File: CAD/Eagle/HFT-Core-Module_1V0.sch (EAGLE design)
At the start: 295 parts, among them Q0521 ABS07-32.768KHZ, Q0911 ABM3B-16MHZ-10-R50-1-U, U0111 STM32L4Z_144PIN_SMPS, U0431 PAM2305AAB120, U0601 LM4120IM5-3.0, U0611 MAX5217, U0631 CFPT-141-20MHZ, U0641 OPA354, U0701 SI5338, U0801 NHD-C0220BIZ_2X20CHARS, U0901 AX5243, U1001 AX5243, U1111 MAX5136AGTG+, U1121 OPA354, U1131 OPA354, U1141 OPA354, U1601 SOLARPANEL_3V3_5MA1_25MM_X_20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, U1602 SPV1040T, U1701 TS5A23166, U1801 PAM2305AAB330, U1901 TS5A23166, U2001 TS5A23166, U2101 TS5A23166, X1501 CUI SJ1-3535NS, X1511 CUI SJ1-3535NS, X511 2X20/90_1MM27_HARWIN_M50-3202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, X512 2X20/90_1MM27_HARWIN_M50-3202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, X521 2X20/90_1MM27_HARWIN_M50-3202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, X522 2X20/90_1MM27_HARWIN_M50-3202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, X531 2X20/90_1MM27_HARWIN_M50-3202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, X532 2X20/90_1MM27_HARWIN_M50-3202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

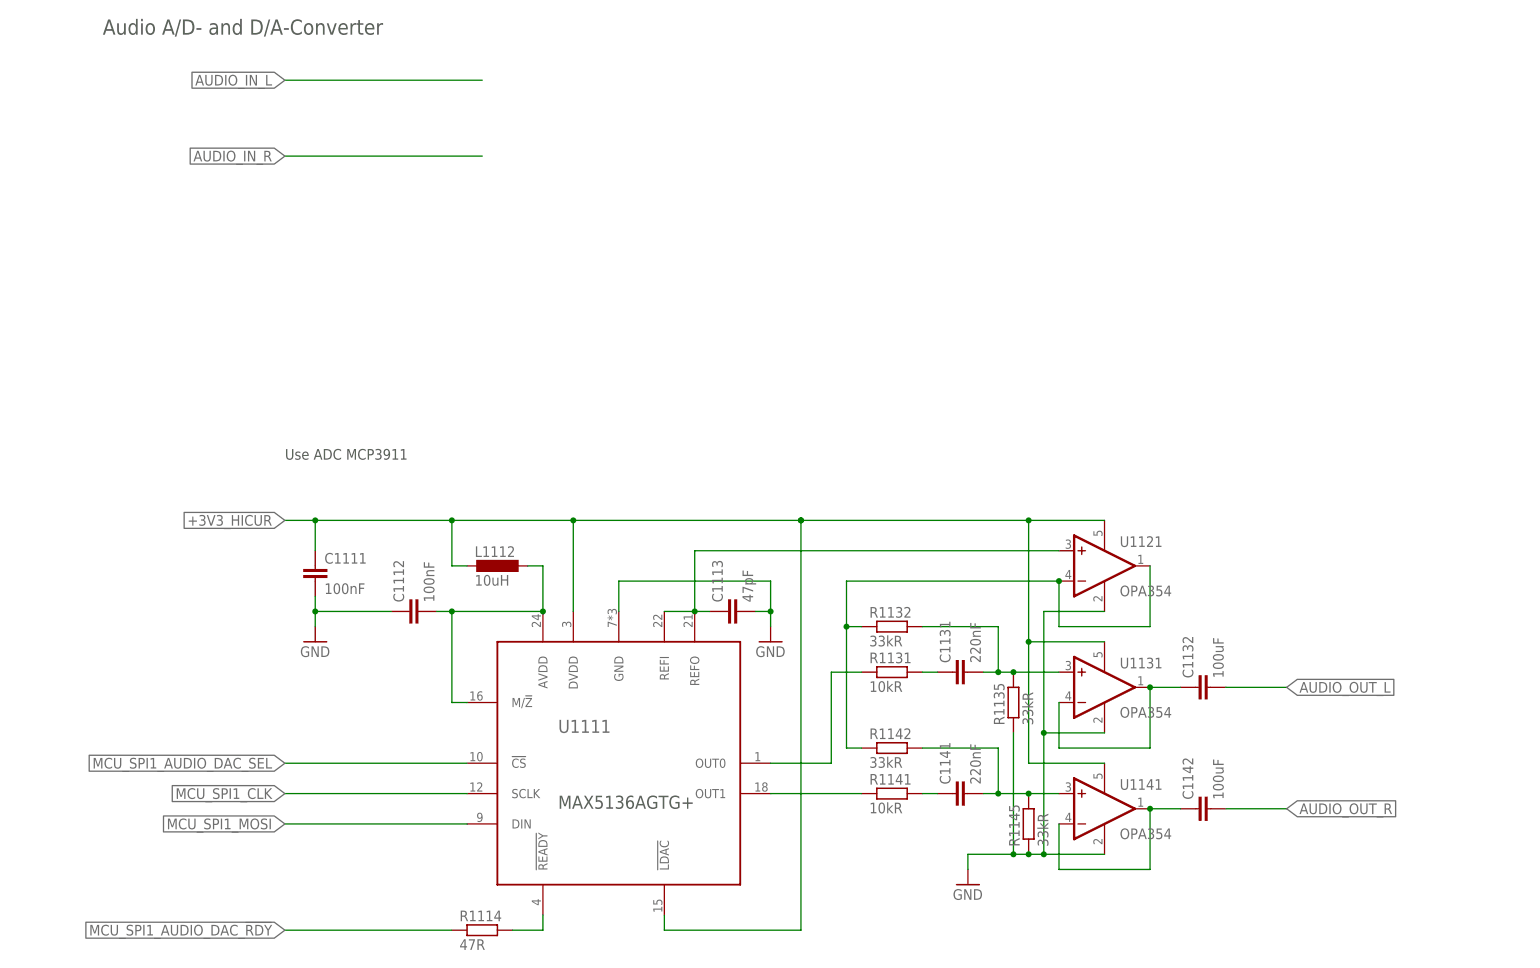
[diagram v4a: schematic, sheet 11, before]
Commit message: HW_1V0 - Audio ADC added
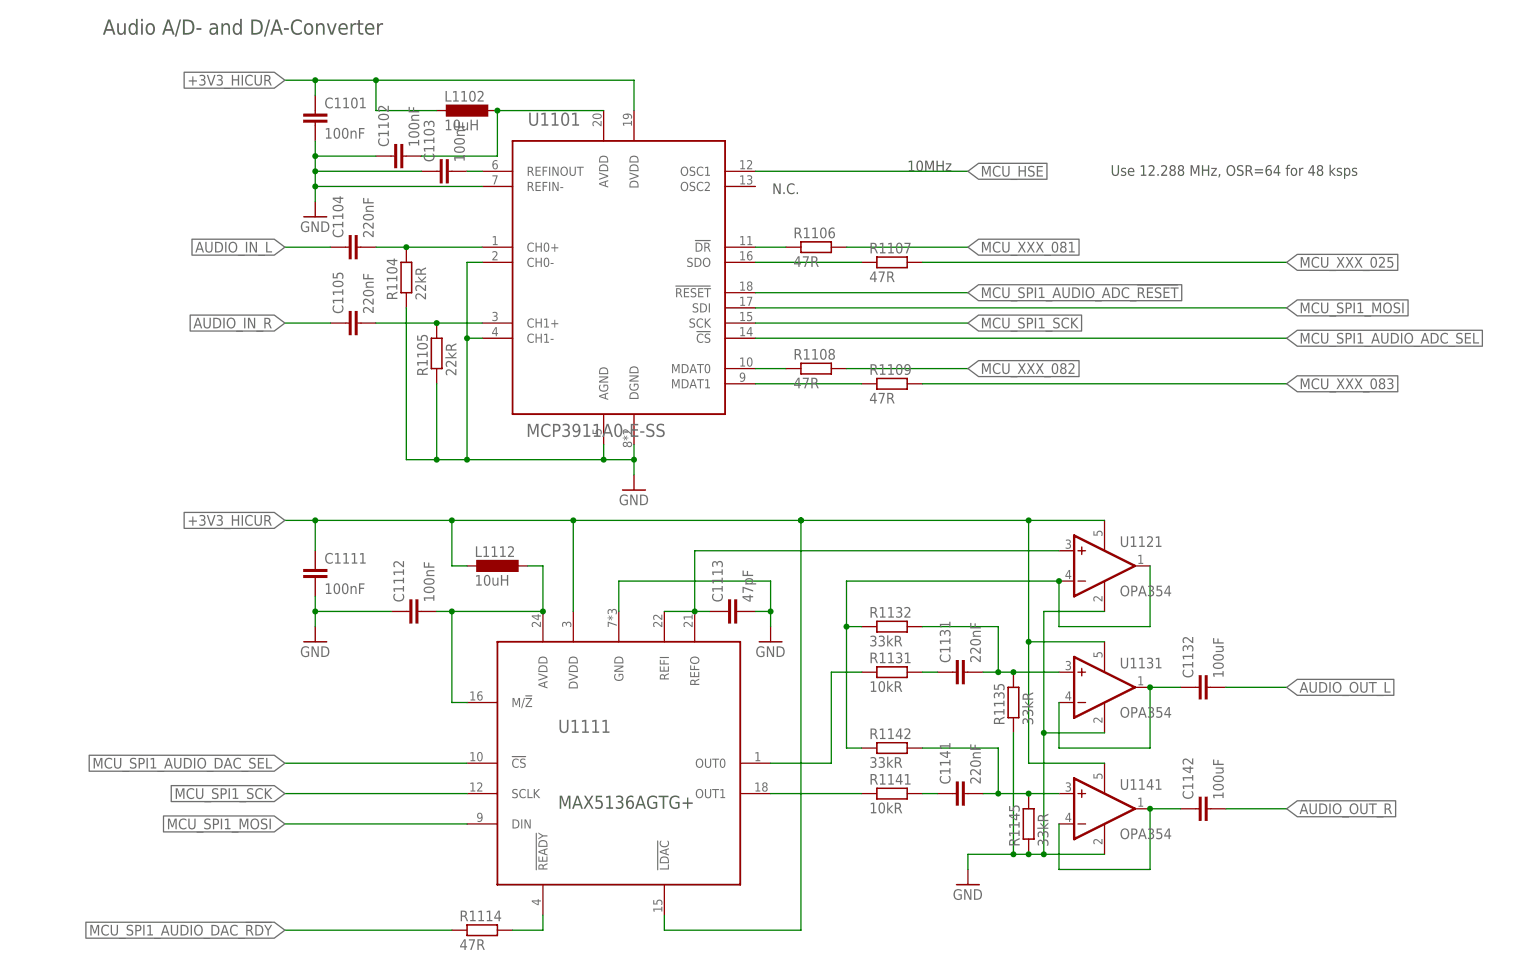
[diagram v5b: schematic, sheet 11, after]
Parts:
- removed R0841: 47R, rcl:R-EU_R0603
- added C1101, C1102, C1103: 100nF, rcl:C-EUC0603
- added C1104, C1105: 220nF, df4iah_rcl:C-EUC0603
- added L1102: 10uH, rcl:L-EUL2012C
- added R0003, R0004, R1106, R1107, R1108, R1109: 47R, rcl:R-EU_R0603
- added R1104, R1105: 22kR, rcl:R-EU_R0603
- added U1101: MCP3911A0-E-SS, df4iah_adc:MCP3911
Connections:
- net N$1 renamed MAX5217_!AUX
- removed net LCD_!RST: R0841.1, U0801.RST
- removed net MCU_SPI1_CLK: R0211.2, U0901.CLK, U1001.CLK, U1111.SCLK
- new net MCP3911_!DR: R1106.1, U1101.!DR
- new net MCP3911_CH0+: C1104.2, R1104.2, U1101.CH0+
- new net MCP3911_CH1+: C1105.2, R1105.2, U1101.CH1+
- new net MCP3911_MDAT0: R1108.1, U1101.MDAT0
- new net MCP3911_MDAT1: R1109.1, U1101.MDAT1
- new net MCP3911_REFINOUT: C1103.2, U1101.REFINOUT
- new net MCP3911_SDO: R1107.1, U1101.SDO
- new net MCU_SPI1_AUDIO_ADC_!RESET: R0003.2, U1101.!RESET
- new net MCU_SPI1_AUDIO_ADC_SEL: R0004.2, U1101.!CS
- new net MCU_SPI1_SCK: R0211.2, U0901.CLK, U1001.CLK, U1101.SCK, U1111.SCLK
- new net MCU_XXX_081: R1106.2
- new net MCU_XXX_082: R1108.2
- new net MCU_XXX_083: R1109.2
- new net MCU_XXX_084: R0003.1
- new net MCU_XXX_085: R0004.1
- new net MVP3911_AVDD: C1102.2, L1102.1, U1101.AVDD
- net +3V3_HICUR: now also C1101.1, L1102.2, U1101.DVDD
- net AUDIO_IN_L: now also C1104.1
- net AUDIO_IN_R: now also C1105.1
- net GND: now also C1101.2, C1102.1, C1103.1, R1104.1, R1105.1, U1101.AGND, U1101.CH0-, U1101.CH1-, U1101.DGND, U1101.REFIN-
- net MCU_HSE: now also U1101.OSC1
- net MCU_LCD_!RST: now also U0801.RST; no longer R0841.2
- net MCU_SPI1_MOSI: now also U1101.SDI
- net MCU_XXX_025: now also R1107.2
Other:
- note added: "10MHz"
- note added: "16MHz"
- note added: "20MHz"
- note added: "MCU_SPI1_AUDIO_ADC_!DR"
- note added: "MCU_SPI1_AUDIO_ADC_M0"
- note added: "MCU_SPI1_AUDIO_ADC_M1"
- note added: "N.C."
- note added: "Use 12.288 MHz, OSR=64 for 48 ksps"
- note removed: "Use ADC MCP3911"
- moved on the sheet: R0642

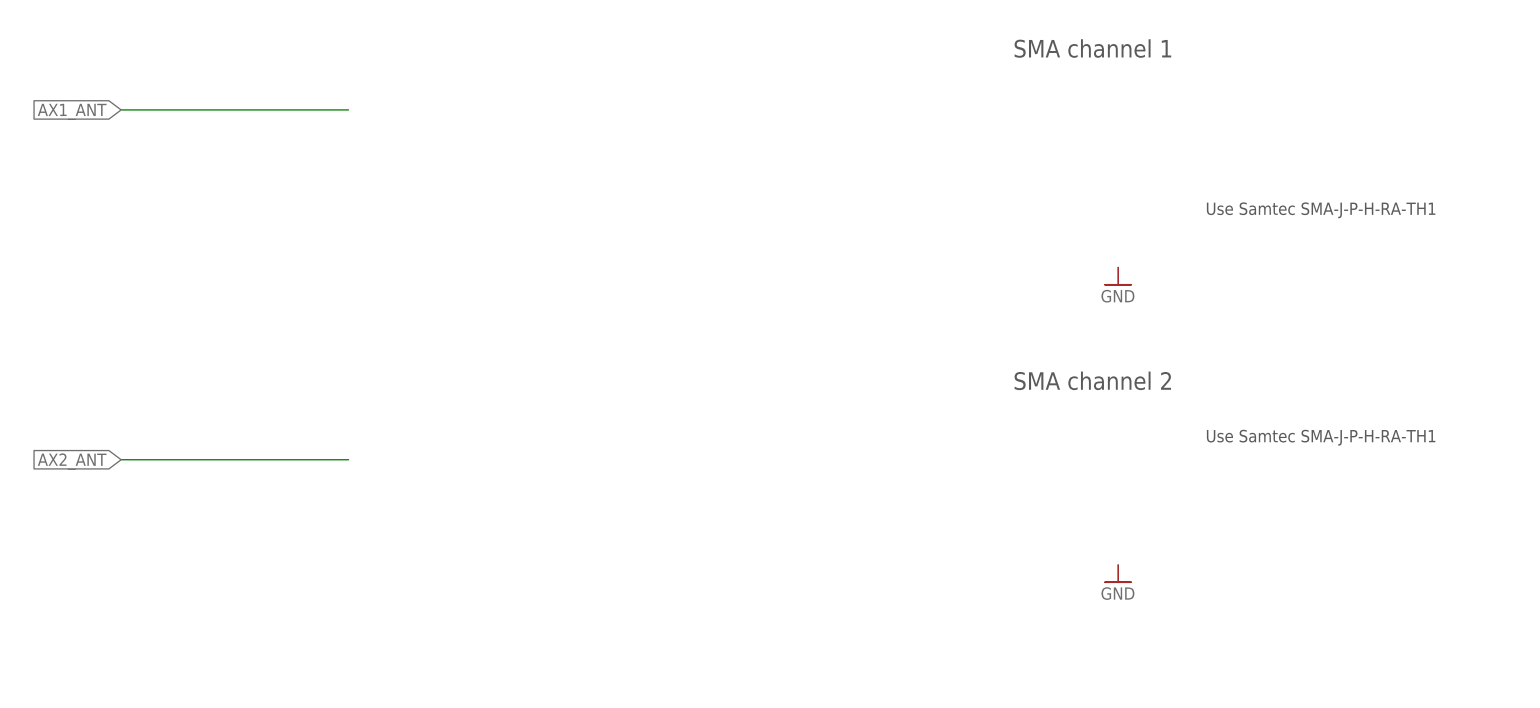
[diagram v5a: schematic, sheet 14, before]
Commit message: HW_1V0 - AX5243 channel 1 and 2 placed, Si5338 placed
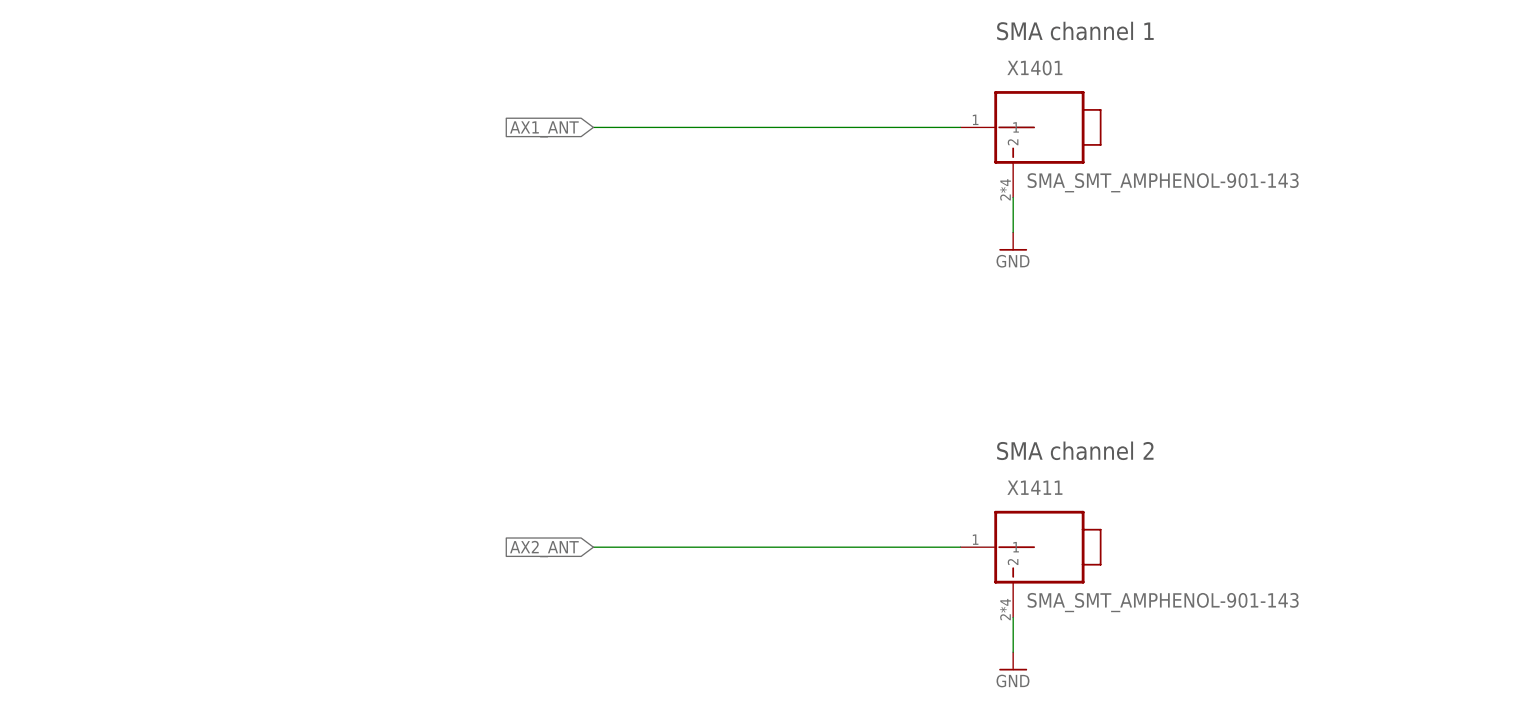
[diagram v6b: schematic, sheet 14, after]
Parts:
- added TP_AX1_IRQ, TP_AX1_TCXO_EN, TP_AX2_IRQ, TP_AX2_TCXO_EN: PTR1TP06R, testpad:PTR1TP06R
- added X1401, X1411: SMA_SMT_AMPHENOL-901-143, df4iah_connector:SMA_SMT_AMPHENOL-901-143
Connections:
- net AX1_ANT: now also X1401.1
- net AX2_ANT: now also X1411.1
- net GND: now also X1401.2, X1411.2
- net MCU_AX1_GPO1: now also TP_AX1_TCXO_EN.TP
- net MCU_AX1_IRQ: now also TP_AX1_IRQ.TP
- net MCU_AX2_GPO1: now also TP_AX2_TCXO_EN.TP
- net MCU_AX2_IRQ: now also TP_AX2_IRQ.TP
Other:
- note removed: "Use Samtec SMA-J-P-H-RA-TH1"
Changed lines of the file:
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@@
 <part name="R1104" library="rcl" deviceset="R-EU_" device="R0603" value="22kR"/>
 <part name="R1105" library="rcl" deviceset="R-EU_" device="R0603" value="22kR"/>
+<part name="X1401" library="df4iah_connector" deviceset="SMA_SMT_AMPHENOL-901-143" device=""/>
+<part name="X1411" library="df4iah_connector" deviceset="SMA_SMT_AMPHENOL-901-143" device=""/>
+<part name="TP_AX2_TCXO_EN" library="testpad" deviceset="PTR1" device="TP06R"/>
+<part name="TP_AX2_IRQ" library="testpad" deviceset="PTR1" device="TP06R"/>
+<part name="TP_AX1_TCXO_EN" library="testpad" deviceset="PTR1" device="TP06R"/>
+<part name="TP_AX1_IRQ" library="testpad" deviceset="PTR1" device="TP06R"/>
 </parts>
 <sheets>
@@
 <instance part="C_AX1_A3" gate="G$1" x="213.36" y="71.12"/>
 <instance part="GND0991" gate="1" x="208.28" y="58.42"/>
+<instance part="TP_AX1_TCXO_EN" gate="G$1" x="58.42" y="53.34"/>
+<instance part="TP_AX1_IRQ" gate="G$1" x="50.8" y="53.34"/>
 </instances>
 <busses>
@@
 <segment>
 <pinref part="U0901" gate="A" pin="IRQ"/>
-<wire x1="60.96" y1="78.74" x2="45.72" y2="78.74" width="0.1524" layer="91"/>
+<wire x1="60.96" y1="78.74" x2="50.8" y2="78.74" width="0.1524" layer="91"/>
 <pinref part="R0951" gate="G$1" pin="2"/>
 <label x="43.18" y="78.74" size="1.778" layer="95"/>
+<pinref part="TP_AX1_IRQ" gate="G$1" pin="TP"/>
+<wire x1="50.8" y1="78.74" x2="45.72" y2="78.74" width="0.1524" layer="91"/>
+<wire x1="50.8" y1="78.74" x2="50.8" y2="55.88" width="0.1524" layer="91"/>
+<junction x="50.8" y="78.74"/>
 </segment>
 </net>
@@
 <pinref part="R0961" gate="G$1" pin="2"/>
 <pinref part="U0901" gate="A" pin="TCXO_EN"/>
-<wire x1="45.72" y1="73.66" x2="60.96" y2="73.66" width="0.1524" layer="91"/>
+<wire x1="45.72" y1="73.66" x2="58.42" y2="73.66" width="0.1524" layer="91"/>
 <label x="43.18" y="73.66" size="1.778" layer="95"/>
+<pinref part="TP_AX1_TCXO_EN" gate="G$1" pin="TP"/>
+<wire x1="58.42" y1="73.66" x2="60.96" y2="73.66" width="0.1524" layer="91"/>
+<wire x1="58.42" y1="73.66" x2="58.42" y2="55.88" width="0.1524" layer="91"/>
+<junction x="58.42" y="73.66"/>
 </segment>
 </net>
@@
 <instance part="GND0001" gate="1" x="114.3" y="114.3"/>
 <instance part="C1011" gate="G$1" x="114.3" y="137.16"/>
+<instance part="TP_AX2_TCXO_EN" gate="G$1" x="58.42" y="53.34"/>
+<instance part="TP_AX2_IRQ" gate="G$1" x="50.8" y="53.34"/>
 </instances>
 <busses>
@@
 <pinref part="R1061" gate="G$1" pin="2"/>
 <pinref part="U1001" gate="A" pin="TCXO_EN"/>
-<wire x1="45.72" y1="73.66" x2="60.96" y2="73.66" width="0.1524" layer="91"/>
+<wire x1="45.72" y1="73.66" x2="58.42" y2="73.66" width="0.1524" layer="91"/>
 <label x="43.18" y="73.66" size="1.778" layer="95"/>
+<wire x1="58.42" y1="73.66" x2="60.96" y2="73.66" width="0.1524" layer="91"/>
+<pinref part="TP_AX2_TCXO_EN" gate="G$1" pin="TP"/>
+<wire x1="58.42" y1="73.66" x2="58.42" y2="55.88" width="0.1524" layer="91"/>
+<junction x="58.42" y="73.66"/>
 </segment>
 </net>
@@
 <segment>
 <pinref part="U1001" gate="A" pin="IRQ"/>
-<wire x1="60.96" y1="78.74" x2="45.72" y2="78.74" width="0.1524" layer="91"/>
+<wire x1="60.96" y1="78.74" x2="50.8" y2="78.74" width="0.1524" layer="91"/>
 <pinref part="R1051" gate="G$1" pin="2"/>
 <label x="43.18" y="78.74" size="1.778" layer="95"/>
+<pinref part="TP_AX2_IRQ" gate="G$1" pin="TP"/>
+<wire x1="50.8" y1="78.74" x2="45.72" y2="78.74" width="0.1524" layer="91"/>
+<wire x1="50.8" y1="78.74" x2="50.8" y2="55.88" width="0.1524" layer="91"/>
+<junction x="50.8" y="78.74"/>
 </segment>
 </net>
@@
 <description>SMA sockets</description>
 <plain>
-<text x="190.5" y="78.74" size="1.778" layer="97">Use Samtec SMA-J-P-H-RA-TH1</text>
-<text x="190.5" y="111.76" size="1.778" layer="97">Use Samtec SMA-J-P-H-RA-TH1</text>
-<text x="162.56" y="134.62" size="2.54" layer="97" ratio="15">SMA channel 1</text>
-<text x="162.56" y="86.36" size="2.54" layer="97" ratio="15">SMA channel 2</text>
+<text x="160.02" y="137.16" size="2.54" layer="97" ratio="15">SMA channel 1</text>
+<text x="160.02" y="76.2" size="2.54" layer="97" ratio="15">SMA channel 2</text>
 </plain>
 <instances>
 <instance part="FRAME15" gate="G$1" x="0" y="0"/>
-<instance part="GND1401" gate="1" x="177.8" y="101.6"/>
-<instance part="GND1411" gate="1" x="177.8" y="58.42"/>
+<instance part="GND1401" gate="1" x="162.56" y="106.68"/>
+<instance part="GND1411" gate="1" x="162.56" y="45.72"/>
+<instance part="X1401" gate="A" x="165.1" y="124.46"/>
+<instance part="X1411" gate="A" x="165.1" y="63.5"/>
 </instances>
 <busses>
@@
 <net name="AX1_ANT" class="0">
 <segment>
-<wire x1="33.02" y1="127" x2="66.04" y2="127" width="0.1524" layer="91"/>
-<label x="33.02" y="127" size="1.778" layer="95" rot="R180" xref="yes"/>
+<wire x1="101.6" y1="124.46" x2="154.94" y2="124.46" width="0.1524" layer="91"/>
+<label x="101.6" y="124.46" size="1.778" layer="95" rot="R180" xref="yes"/>
+<pinref part="X1401" gate="A" pin="1"/>
 </segment>
 </net>
 <net name="AX2_ANT" class="0">
 <segment>
-<wire x1="33.02" y1="76.2" x2="66.04" y2="76.2" width="0.1524" layer="91"/>
-<label x="33.02" y="76.2" size="1.778" layer="95" rot="R180" xref="yes"/>
+<wire x1="101.6" y1="63.5" x2="154.94" y2="63.5" width="0.1524" layer="91"/>
+<label x="101.6" y="63.5" size="1.778" layer="95" rot="R180" xref="yes"/>
+<pinref part="X1411" gate="A" pin="1"/>
+</segment>
+</net>
+<net name="GND" class="0">
+<segment>
+<pinref part="GND1411" gate="1" pin="GND"/>
+<pinref part="X1411" gate="A" pin="2"/>
+<wire x1="162.56" y1="48.26" x2="162.56" y2="53.34" width="0.1524" layer="91"/>
+</segment>
+<segment>
+<pinref part="GND1401" gate="1" pin="GND"/>
+<pinref part="X1401" gate="A" pin="2"/>
+<wire x1="162.56" y1="109.22" x2="162.56" y2="114.3" width="0.1524" layer="91"/>
 </segment>
 </net>

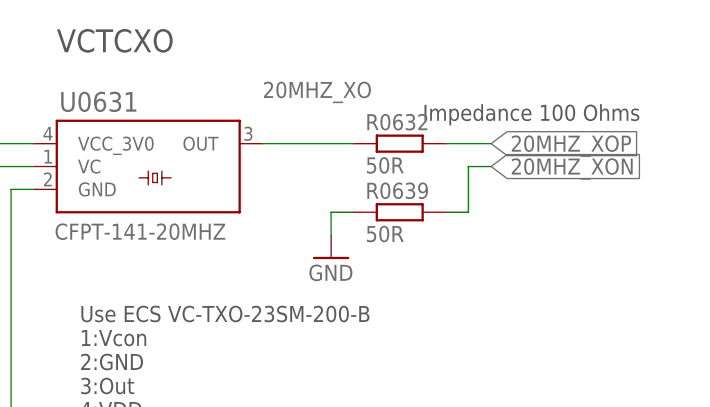
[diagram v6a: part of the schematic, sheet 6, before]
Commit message: HW_1V0 - TCXO placed
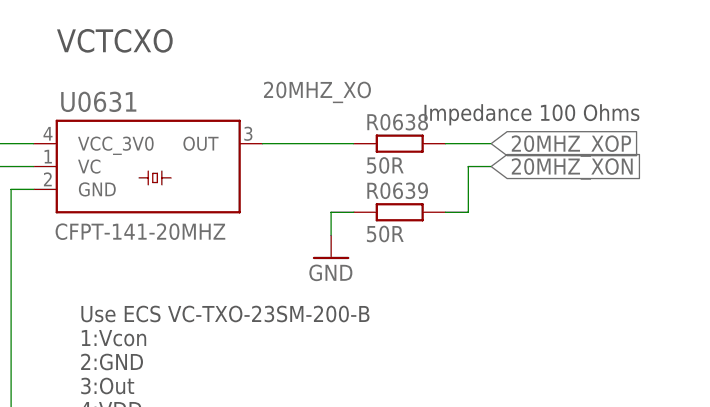
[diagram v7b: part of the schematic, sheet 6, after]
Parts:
- renumbered R0632 to R0638
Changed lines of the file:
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@@
 <part name="C0715" library="rcl" deviceset="C-EU" device="C0603" value="10nF"/>
 <part name="C0716" library="rcl" deviceset="C-EU" device="C0603" value="10nF"/>
-<part name="R0632" library="rcl" deviceset="R-EU_" device="R0603" value="50R"/>
+<part name="R0638" library="rcl" deviceset="R-EU_" device="R0603" value="50R"/>
 <part name="R0639" library="rcl" deviceset="R-EU_" device="R0603" value="50R"/>
 <part name="GND0632" library="df4iah_supply" deviceset="GND" device=""/>
@@
 <instance part="R0613" gate="G$1" x="25.4" y="152.4"/>
 <instance part="C0611" gate="G$1" x="76.2" y="142.24"/>
-<instance part="R0632" gate="G$1" x="220.98" y="160.02"/>
+<instance part="R0638" gate="G$1" x="220.98" y="160.02"/>
 <instance part="R0639" gate="G$1" x="220.98" y="152.4"/>
 <instance part="GND0632" gate="1" x="213.36" y="147.32"/>
@@
 <pinref part="U0631" gate="&gt;NAME" pin="OUT"/>
 <wire x1="205.74" y1="160.02" x2="215.9" y2="160.02" width="0.1524" layer="91"/>
-<pinref part="R0632" gate="G$1" pin="1"/>
+<pinref part="R0638" gate="G$1" pin="1"/>
 <label x="205.74" y="165.1" size="1.778" layer="95"/>
 </segment>
@@
 <net name="20MHZ_XOP" class="0">
 <segment>
-<pinref part="R0632" gate="G$1" pin="2"/>
+<pinref part="R0638" gate="G$1" pin="2"/>
 <wire x1="226.06" y1="160.02" x2="231.14" y2="160.02" width="0.1524" layer="91"/>
 <label x="231.14" y="160.02" size="1.778" layer="95" xref="yes"/>
